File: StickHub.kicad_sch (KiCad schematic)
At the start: 94 parts, among them J1 HOST, J2 USB1, J3 USB2, J4 USB3, J5 USB4, J6 USB5, J7 USB6, J8 USB7, J9 EXTGND, U1 MaxLinear_XR22417-48, U2 Dialog_SLG5NT1487V, Y1 12MHz 50ppm 16-20pF

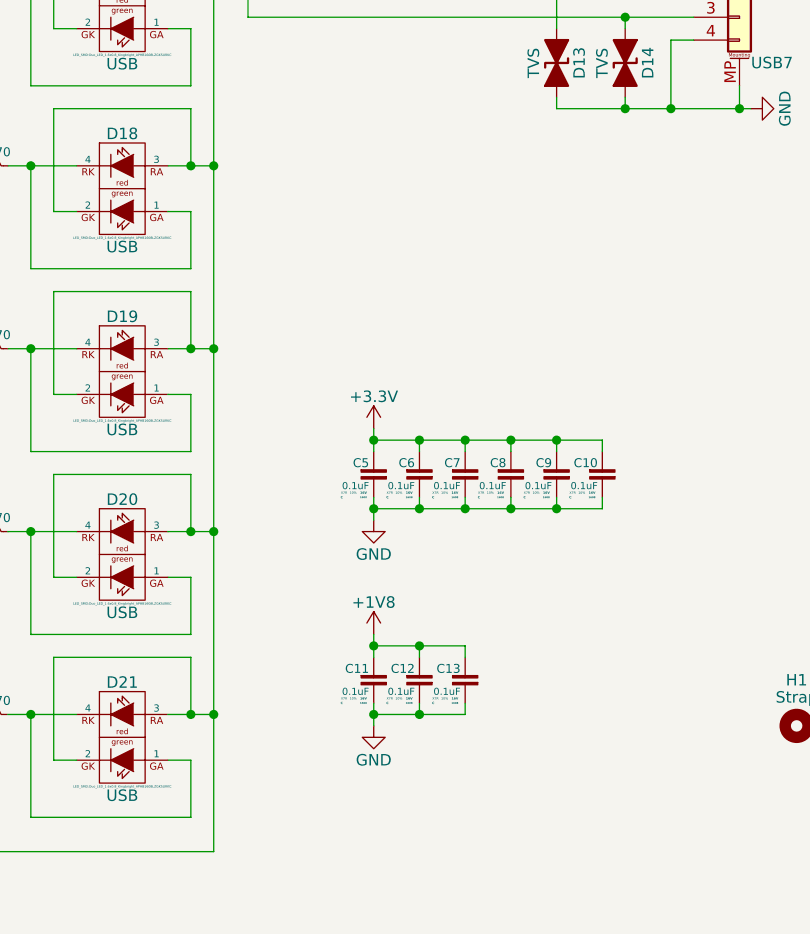
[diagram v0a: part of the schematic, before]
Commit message: Changing capacitor values.
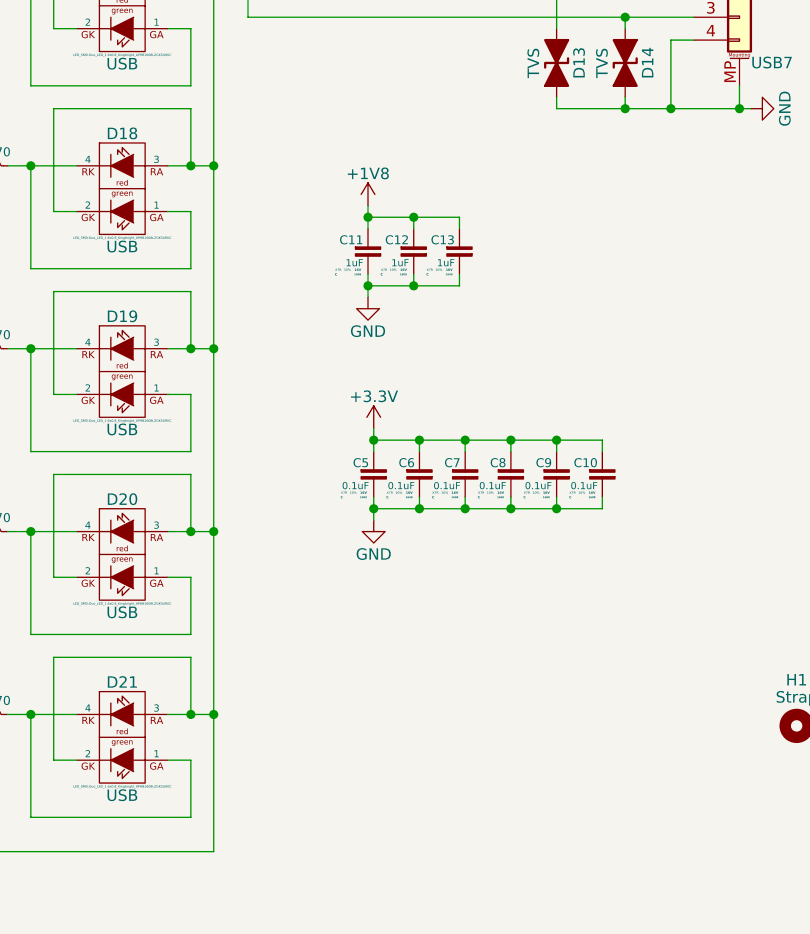
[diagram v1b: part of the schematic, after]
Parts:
- C11, C12, C13: value 0.1uF -> 1uF
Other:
- moved on the sheet: C11, C12, C13
